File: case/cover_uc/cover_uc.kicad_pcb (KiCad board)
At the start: 2 copper layers, 31 x 71.2 mm, 0 parts

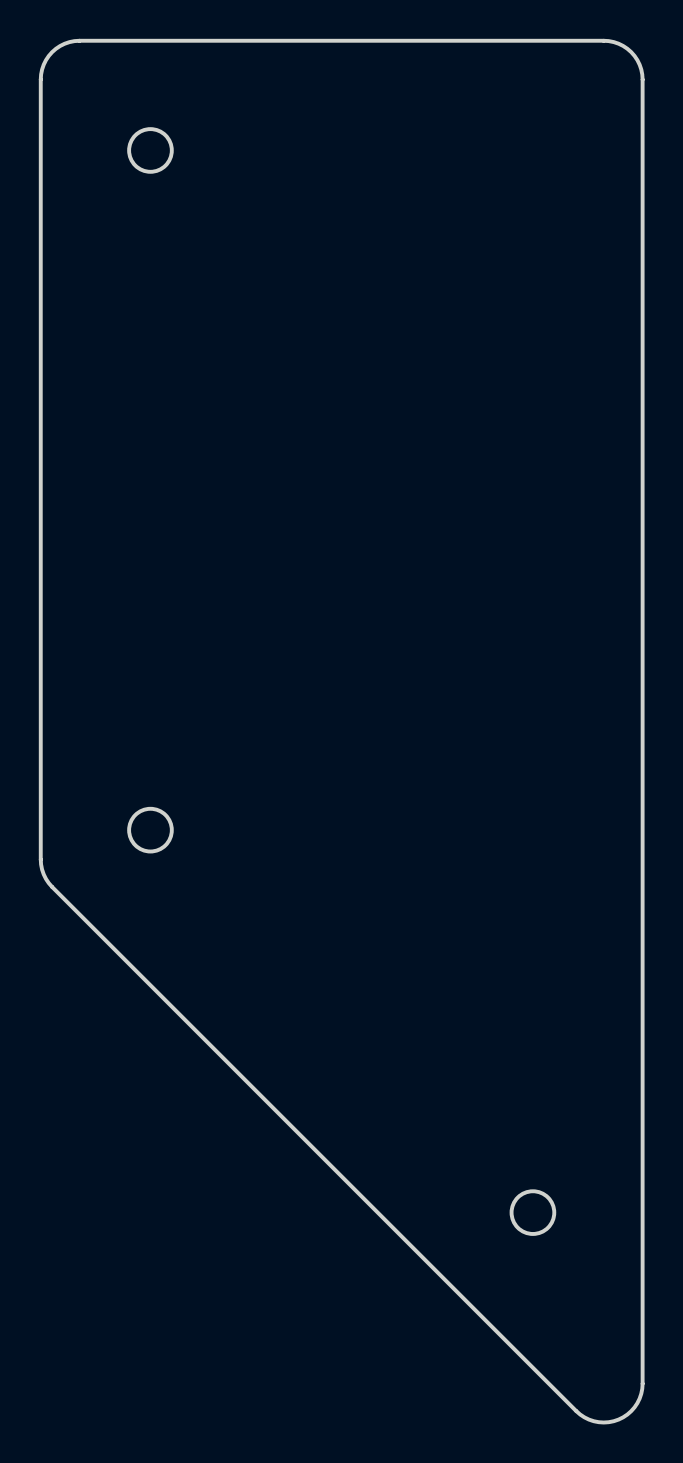
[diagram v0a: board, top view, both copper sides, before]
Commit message: Circles to holes
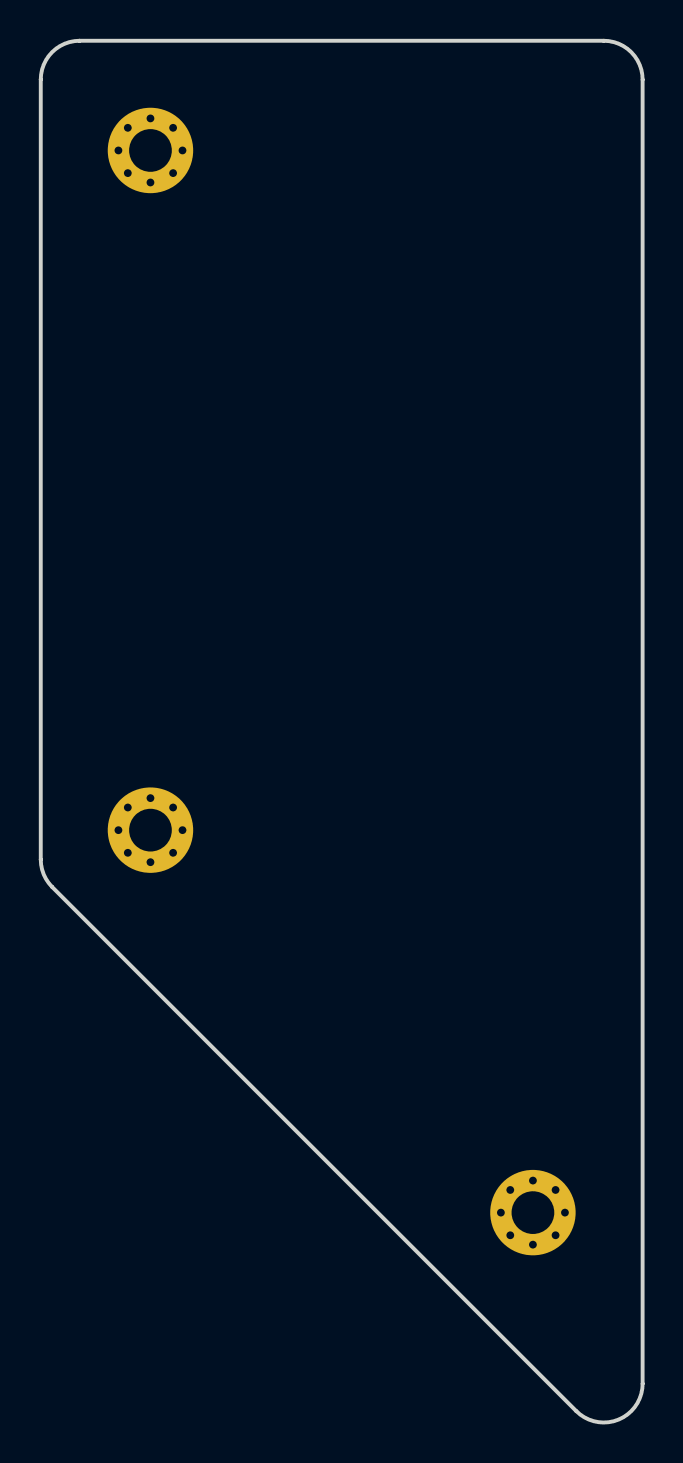
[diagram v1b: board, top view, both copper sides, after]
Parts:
- added REF**: MountingHole_2.2mm_M2_Pad_Via, MountingHole_2.2mm_M2_Pad_Via, F.Cu at (61.6, 42.6)
- added REF**: MountingHole_2.2mm_M2_Pad_Via, MountingHole_2.2mm_M2_Pad_Via, F.Cu at (61.6, 77.7)
- added REF**: MountingHole_2.2mm_M2_Pad_Via, MountingHole_2.2mm_M2_Pad_Via, F.Cu at (81.3, 97.4)
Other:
- outline, holes or cut-outs redrawn
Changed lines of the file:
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@@
     (tracks 0)
     (zones 0)
-    (modules 0)
+    (modules 3)
     (nets 1)
   )
@@
     (uvia_drill 0.1)
   )
-  (gr_circle (center 81.35 97.359693) (end 82.449999 97.359693) (layer Edge.Cuts) (width 0.2))
-  (gr_circle (center 61.65 77.659693) (end 62.75 77.659693) (layer Edge.Cuts) (width 0.2))
-  (gr_circle (center 61.65 42.65) (end 62.75 42.65) (layer Edge.Cuts) (width 0.2))
+  (module MountingHole_2.2mm_M2_Pad_Via (layer F.Cu)
+    (at 61.65 42.65)
+    (descr "Mounting Hole 2.2mm, M2")
+    (tags "mounting hole 2.2mm m2")
+    (attr virtual)
+    (fp_text reference REF** (at 0 -3.2) (layer F.SilkS) hide
+      (effects (font (size 1 1) (thickness 0.15)))
+    )
+    (fp_text value MountingHole_2.2mm_M2_Pad_Via (at 0 3.2) (layer F.Fab)
+      (effects (font (size 1 1) (thickness 0.15)))
+    )
+    (fp_circle (center 0 0) (end 2.45 0) (layer F.CrtYd) (width 0.05))
+    (fp_circle (center 0 0) (end 2.2 0) (layer Cmts.User) (width 0.15))
+    (fp_text user %R (at 0.3 0) (layer F.Fab)
+      (effects (font (size 1 1) (thickness 0.15)))
+    )
+    (pad 1 thru_hole circle (at 1.166726 -1.166726) (size 0.7 0.7) (drill 0.4) (layers *.Cu *.Mask))
+    (pad 1 thru_hole circle (at 0 -1.65) (size 0.7 0.7) (drill 0.4) (layers *.Cu *.Mask))
+    (pad 1 thru_hole circle (at -1.166726 -1.166726) (size 0.7 0.7) (drill 0.4) (layers *.Cu *.Mask))
+    (pad 1 thru_hole circle (at -1.65 0) (size 0.7 0.7) (drill 0.4) (layers *.Cu *.Mask))
+    (pad 1 thru_hole circle (at -1.166726 1.166726) (size 0.7 0.7) (drill 0.4) (layers *.Cu *.Mask))
+    (pad 1 thru_hole circle (at 0 1.65) (size 0.7 0.7) (drill 0.4) (layers *.Cu *.Mask))
+    (pad 1 thru_hole circle (at 1.166726 1.166726) (size 0.7 0.7) (drill 0.4) (layers *.Cu *.Mask))
+    (pad 1 thru_hole circle (at 1.65 0) (size 0.7 0.7) (drill 0.4) (layers *.Cu *.Mask))
+    (pad 1 thru_hole circle (at 0 0) (size 4.4 4.4) (drill 2.2) (layers *.Cu *.Mask))
+  )
+  (module MountingHole_2.2mm_M2_Pad_Via (layer F.Cu)
+    (at 61.65 77.659693)
+    (descr "Mounting Hole 2.2mm, M2")
+    (tags "mounting hole 2.2mm m2")
+    (attr virtual)
+    (fp_text reference REF** (at 0 -3.2) (layer F.SilkS) hide
+      (effects (font (size 1 1) (thickness 0.15)))
+    )
+    (fp_text value MountingHole_2.2mm_M2_Pad_Via (at 0 3.2) (layer F.Fab)
+      (effects (font (size 1 1) (thickness 0.15)))
+    )
+    (fp_circle (center 0 0) (end 2.45 0) (layer F.CrtYd) (width 0.05))
+    (fp_circle (center 0 0) (end 2.2 0) (layer Cmts.User) (width 0.15))
+    (fp_text user %R (at 0.3 0) (layer F.Fab)
+      (effects (font (size 1 1) (thickness 0.15)))
+    )
+    (pad 1 thru_hole circle (at 1.166726 -1.166726) (size 0.7 0.7) (drill 0.4) (layers *.Cu *.Mask))
+    (pad 1 thru_hole circle (at 0 -1.65) (size 0.7 0.7) (drill 0.4) (layers *.Cu *.Mask))
+    (pad 1 thru_hole circle (at -1.166726 -1.166726) (size 0.7 0.7) (drill 0.4) (layers *.Cu *.Mask))
+    (pad 1 thru_hole circle (at -1.65 0) (size 0.7 0.7) (drill 0.4) (layers *.Cu *.Mask))
+    (pad 1 thru_hole circle (at -1.166726 1.166726) (size 0.7 0.7) (drill 0.4) (layers *.Cu *.Mask))
+    (pad 1 thru_hole circle (at 0 1.65) (size 0.7 0.7) (drill 0.4) (layers *.Cu *.Mask))
+    (pad 1 thru_hole circle (at 1.166726 1.166726) (size 0.7 0.7) (drill 0.4) (layers *.Cu *.Mask))
+    (pad 1 thru_hole circle (at 1.65 0) (size 0.7 0.7) (drill 0.4) (layers *.Cu *.Mask))
+    (pad 1 thru_hole circle (at 0 0) (size 4.4 4.4) (drill 2.2) (layers *.Cu *.Mask))
+  )
+  (module MountingHole_2.2mm_M2_Pad_Via (layer F.Cu)
+    (at 81.35 97.359693)
+    (descr "Mounting Hole 2.2mm, M2")
+    (tags "mounting hole 2.2mm m2")
+    (attr virtual)
+    (fp_text reference REF** (at 0 -3.2) (layer F.SilkS) hide
+      (effects (font (size 1 1) (thickness 0.15)))
+    )
+    (fp_text value MountingHole_2.2mm_M2_Pad_Via (at 0 3.2) (layer F.Fab)
+      (effects (font (size 1 1) (thickness 0.15)))
+    )
+    (fp_circle (center 0 0) (end 2.45 0) (layer F.CrtYd) (width 0.05))
+    (fp_circle (center 0 0) (end 2.2 0) (layer Cmts.User) (width 0.15))
+    (fp_text user %R (at 0.3 0) (layer F.Fab)
+      (effects (font (size 1 1) (thickness 0.15)))
+    )
+    (pad 1 thru_hole circle (at 1.166726 -1.166726) (size 0.7 0.7) (drill 0.4) (layers *.Cu *.Mask))
+    (pad 1 thru_hole circle (at 0 -1.65) (size 0.7 0.7) (drill 0.4) (layers *.Cu *.Mask))
+    (pad 1 thru_hole circle (at -1.166726 -1.166726) (size 0.7 0.7) (drill 0.4) (layers *.Cu *.Mask))
+    (pad 1 thru_hole circle (at -1.65 0) (size 0.7 0.7) (drill 0.4) (layers *.Cu *.Mask))
+    (pad 1 thru_hole circle (at -1.166726 1.166726) (size 0.7 0.7) (drill 0.4) (layers *.Cu *.Mask))
+    (pad 1 thru_hole circle (at 0 1.65) (size 0.7 0.7) (drill 0.4) (layers *.Cu *.Mask))
+    (pad 1 thru_hole circle (at 1.166726 1.166726) (size 0.7 0.7) (drill 0.4) (layers *.Cu *.Mask))
+    (pad 1 thru_hole circle (at 1.65 0) (size 0.7 0.7) (drill 0.4) (layers *.Cu *.Mask))
+    (pad 1 thru_hole circle (at 0 0) (size 4.4 4.4) (drill 2.2) (layers *.Cu *.Mask))
+  )
+  (gr_circle (center 81.35 97.359693) (end 82.449999 97.359693) (layer Eco1.User) (width 0.2))
+  (gr_circle (center 61.65 77.659693) (end 62.75 77.659693) (layer Eco1.User) (width 0.2))
+  (gr_circle (center 61.65 42.65) (end 62.75 42.65) (layer Eco1.User) (width 0.2))
   (gr_arc (start 58 39) (end 58 37) (angle -90) (layer Edge.Cuts) (width 0.2))
   (gr_line (start 85 37) (end 58 37) (layer Edge.Cuts) (width 0.2))

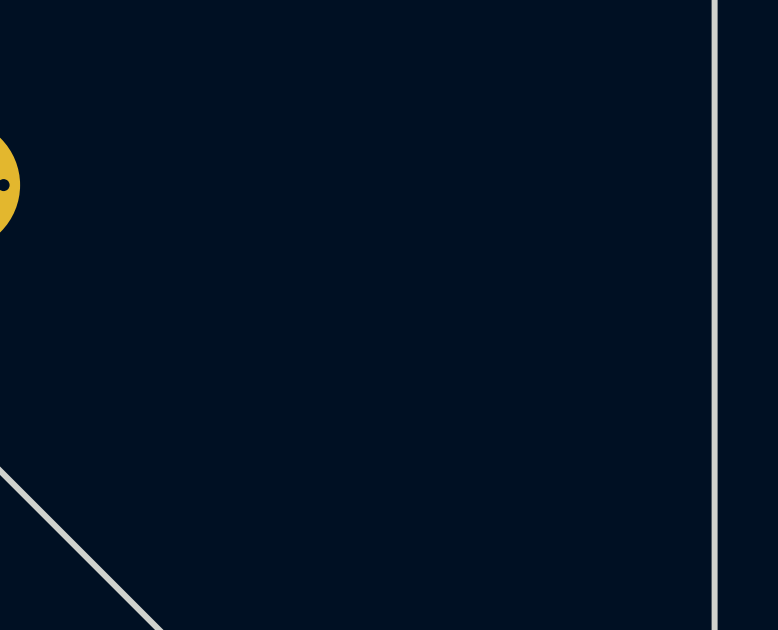
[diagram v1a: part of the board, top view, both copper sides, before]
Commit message: Add reset hole in uc cover
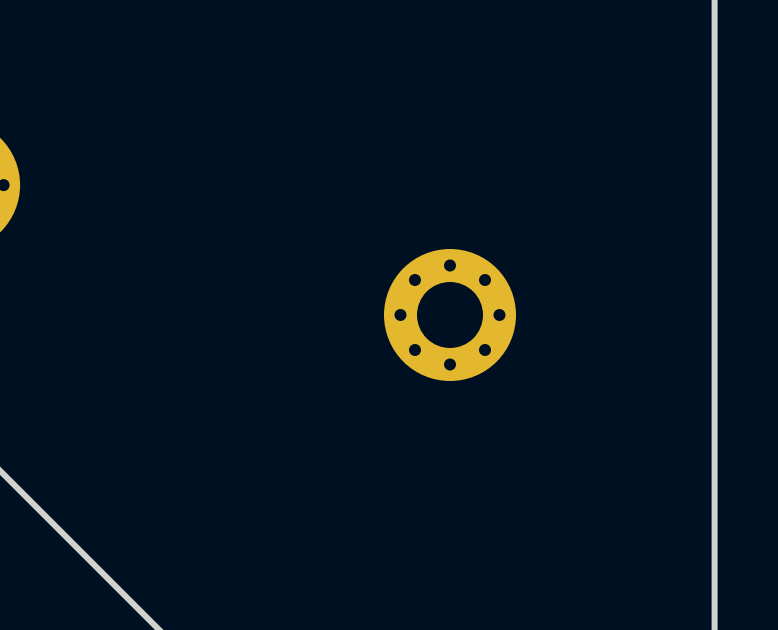
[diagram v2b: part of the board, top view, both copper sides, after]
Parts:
- added REF**: MountingHole_2.2mm_M2_Pad_Via, MountingHole_2.2mm_M2_Pad_Via, F.Cu at (78.2, 82.0)
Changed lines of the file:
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@@
   (general
     (thickness 1.6)
-    (drawings 11)
+    (drawings 12)
     (tracks 0)
     (zones 0)
-    (modules 3)
+    (modules 4)
     (nets 1)
   )
@@
   )
   (module MountingHole_2.2mm_M2_Pad_Via (layer F.Cu)
+    (at 78.18 81.99)
+    (descr "Mounting Hole 2.2mm, M2")
+    (tags "mounting hole 2.2mm m2")
+    (attr virtual)
+    (fp_text reference REF** (at 0 -3.2) (layer F.SilkS) hide
+      (effects (font (size 1 1) (thickness 0.15)))
+    )
+    (fp_text value MountingHole_2.2mm_M2_Pad_Via (at 0 3.2) (layer F.Fab)
+      (effects (font (size 1 1) (thickness 0.15)))
+    )
+    (fp_circle (center 0 0) (end 2.45 0) (layer F.CrtYd) (width 0.05))
+    (fp_circle (center 0 0) (end 2.2 0) (layer Cmts.User) (width 0.15))
+    (fp_text user %R (at 0.3 0) (layer F.Fab)
+      (effects (font (size 1 1) (thickness 0.15)))
+    )
+    (pad 1 thru_hole circle (at 1.166726 -1.166726) (size 0.7 0.7) (drill 0.4) (layers *.Cu *.Mask))
+    (pad 1 thru_hole circle (at 0 -1.65) (size 0.7 0.7) (drill 0.4) (layers *.Cu *.Mask))
+    (pad 1 thru_hole circle (at -1.166726 -1.166726) (size 0.7 0.7) (drill 0.4) (layers *.Cu *.Mask))
+    (pad 1 thru_hole circle (at -1.65 0) (size 0.7 0.7) (drill 0.4) (layers *.Cu *.Mask))
+    (pad 1 thru_hole circle (at -1.166726 1.166726) (size 0.7 0.7) (drill 0.4) (layers *.Cu *.Mask))
+    (pad 1 thru_hole circle (at 0 1.65) (size 0.7 0.7) (drill 0.4) (layers *.Cu *.Mask))
+    (pad 1 thru_hole circle (at 1.166726 1.166726) (size 0.7 0.7) (drill 0.4) (layers *.Cu *.Mask))
+    (pad 1 thru_hole circle (at 1.65 0) (size 0.7 0.7) (drill 0.4) (layers *.Cu *.Mask))
+    (pad 1 thru_hole circle (at 0 0) (size 4.4 4.4) (drill 2.2) (layers *.Cu *.Mask))
+  )
+  (module MountingHole_2.2mm_M2_Pad_Via (layer F.Cu)
     (at 81.35 97.359693)
     (descr "Mounting Hole 2.2mm, M2")
@@
   )
   (gr_circle (center 81.35 97.359693) (end 82.449999 97.359693) (layer Eco1.User) (width 0.2))
+  (gr_circle (center 78.18 81.99) (end 79.28 81.99) (layer Eco1.User) (width 0.2))
   (gr_circle (center 61.65 77.659693) (end 62.75 77.659693) (layer Eco1.User) (width 0.2))
   (gr_circle (center 61.65 42.65) (end 62.75 42.65) (layer Eco1.User) (width 0.2))
